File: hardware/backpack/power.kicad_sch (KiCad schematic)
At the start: 13 parts, among them J6 CONN 2x5 P=2.54mm

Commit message: start power
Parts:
- added U5: AP63200WU, Package_TO_SOT_SMD:TSOT-23-6, symbol Regulator_Switching:AP63200WU
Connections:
- net +12V: now also U5.2 (EN), U5.3 (IN)
- net GND: now also U5.4 (GND)

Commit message: start on regs
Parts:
- added C30, C34, C35: 100nF, Capacitor_SMD:C_0603_1608Metric, symbol Device:C_Small
- added C31: 100pF, Capacitor_SMD:C_0603_1608Metric, symbol Device:C_Small
- added C32, C33: 22.0uF, Capacitor_Tantalum_SMD:CP_EIA-3216-10_Kemet-I, symbol Device:C_Polarized_Small
- added F1, F2: 250mA, symbol Device:Polyfuse_Small
- added L3: 6.8uH 2A, symbol Device:L_Ferrite_Small
- added R17: 182K, Resistor_SMD:R_0402_1005Metric, symbol Device:R
- added R18: 62K, Resistor_SMD:R_0402_1005Metric, symbol Device:R
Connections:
- net GND: now also C32.2, C33.2, C34.2, C35.2, R18.1
- net at J6.1 (Pin_1), J6.2 (Pin_2): now also F2.1; no longer D3.1 (K)
- net at J6.10 (Pin_10), J6.9 (Pin_9): now also F1.1; no longer D2.2 (A)
- net at U5.1 (FB): now also C31.1, R17.1, R18.2
- net at U5.5 (SW): now also C30.2, L3.1
- net at U5.6 (BST): now also C30.1
- new net: D3.1 (K), F2.2
- new net: D2.2 (A), F1.2
- new net +3V3: C31.2, C32.1, C33.1, C34.1, C35.1, L3.2, R17.2
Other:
- moved on the sheet: C22, C23, C24, C25, C26, C27, C28, C29, D2, D3, L1, L2

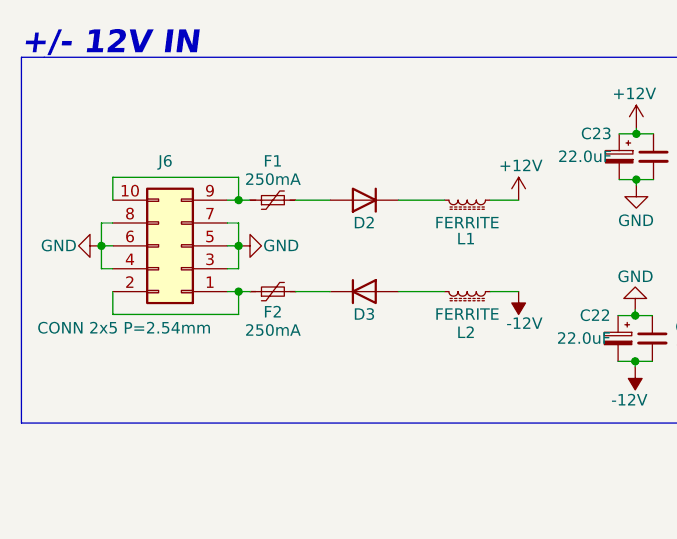
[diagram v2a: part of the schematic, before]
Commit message: parts and capture done sans most needing future pinswaps
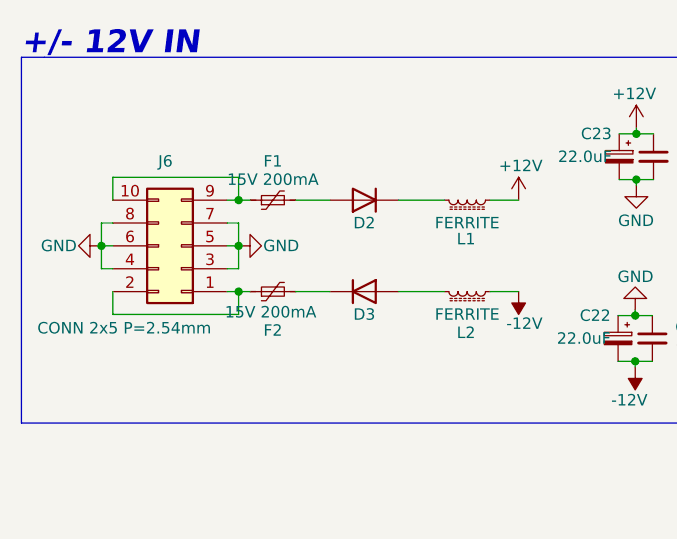
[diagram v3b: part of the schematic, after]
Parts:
- F1, F2: value 250mA -> 15V 200mA; footprint (none) -> Fuse:Fuse_0805_2012Metric; lcsc# (none) -> C883103
- L3: footprint (none) -> Inductor_SMD:L_Vishay_IHLP-2020; lcsc# (none) -> C844992
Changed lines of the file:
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@@
 			)
 		)
-		(property "Footprint" ""
+		(property "Footprint" "Inductor_SMD:L_Vishay_IHLP-2020"
 			(at 86.36 87.63 0)
 			(effects
@@
 			)
 		)
+		(property "lcsc#" " C844992"
+			(at 86.36 87.63 90)
+			(effects
+				(font
+					(size 1.27 1.27)
+				)
+				(hide yes)
+			)
+		)
 		(pin "2"
 		)
@@
 	)
 	(symbol
+		(lib_id "Device:Polyfuse_Small")
+		(at 46.99 46.99 90)
+		(unit 1)
+		(exclude_from_sim no)
+		(in_bom yes)
+		(on_board yes)
+		(dnp no)
+		(property "Reference" "F2"
+			(at 46.99 51.308 90)
+			(effects
+				(font
+					(size 1.27 1.27)
+				)
+			)
+		)
+		(property "Value" "15V 200mA"
+			(at 46.736 49.276 90)
+			(effects
+				(font
+					(size 1.27 1.27)
+				)
+			)
+		)
+		(property "Footprint" "Fuse:Fuse_0805_2012Metric"
+			(at 52.07 45.72 0)
+			(effects
+				(font
+					(size 1.27 1.27)
+				)
+				(justify left)
+				(hide yes)
+			)
+		)
+		(property "Datasheet" "~"
+			(at 46.99 46.99 0)
+			(effects
+				(font
+					(size 1.27 1.27)
+				)
+				(hide yes)
+			)
+		)
+		(property "Description" "Resettable fuse, polymeric positive temperature coefficient, small symbol"
+			(at 46.99 46.99 0)
+			(effects
+				(font
+					(size 1.27 1.27)
+				)
+				(hide yes)
+			)
+		)
+		(property "lcsc#" "C883103"
+			(at 46.99 46.99 90)
+			(effects
+				(font
+					(size 1.27 1.27)
+				)
+				(hide yes)
+			)
+		)
+		(pin "2"
+		)
+		(pin "1"
+		)
+		(instances
+			(project "backpack"
+				(path "/df6062c3-a570-4505-924c-c7fe32df3670/4885642e-e1b2-4a9c-a477-910295b2621e"
+					(reference "F2")
+					(unit 1)
+				)
+			)
+		)
+	)
+	(symbol
 		(lib_id "Device:C_Polarized_Small")
 		(at 85.344 52.197 0)
@@
 	(symbol
 		(lib_id "Device:Polyfuse_Small")
-		(at 46.99 46.99 90)
+		(at 46.99 36.83 90)
 		(unit 1)
 		(exclude_from_sim no)
@@
 		(on_board yes)
 		(dnp no)
-		(property "Reference" "F2"
-			(at 46.99 49.276 90)
+		(property "Reference" "F1"
+			(at 46.99 32.512 90)
 			(effects
 				(font
@@
 			)
 		)
-		(property "Value" "250mA"
-			(at 46.99 51.308 90)
+		(property "Value" "15V 200mA"
+			(at 46.99 34.544 90)
 			(effects
 				(font
@@
 			)
 		)
-		(property "Footprint" ""
-			(at 52.07 45.72 0)
+		(property "Footprint" "Fuse:Fuse_0805_2012Metric"
+			(at 52.07 35.56 0)
 			(effects
 				(font
@@
 		)
 		(property "Datasheet" "~"
-			(at 46.99 46.99 0)
+			(at 46.99 36.83 0)
 			(effects
 				(font
@@
 		)
 		(property "Description" "Resettable fuse, polymeric positive temperature coefficient, small symbol"
-			(at 46.99 46.99 0)
-			(effects
-				(font
-					(size 1.27 1.27)
-				)
-				(hide yes)
-			)
-		)
-		(pin "2"
-		)
-		(pin "1"
-		)
-		(instances
-			(project "backpack"
-				(path "/df6062c3-a570-4505-924c-c7fe32df3670/4885642e-e1b2-4a9c-a477-910295b2621e"
-					(reference "F2")
-					(unit 1)
-				)
-			)
-		)
-	)
-	(symbol
-		(lib_id "Device:Polyfuse_Small")
-		(at 46.99 36.83 90)
-		(unit 1)
-		(exclude_from_sim no)
-		(in_bom yes)
-		(on_board yes)
-		(dnp no)
-		(property "Reference" "F1"
-			(at 46.99 32.512 90)
-			(effects
-				(font
-					(size 1.27 1.27)
-				)
-			)
-		)
-		(property "Value" "250mA"
-			(at 46.99 34.544 90)
-			(effects
-				(font
-					(size 1.27 1.27)
-				)
-			)
-		)
-		(property "Footprint" ""
-			(at 52.07 35.56 0)
-			(effects
-				(font
-					(size 1.27 1.27)
-				)
-				(justify left)
-				(hide yes)
-			)
-		)
-		(property "Datasheet" "~"
 			(at 46.99 36.83 0)
 			(effects
@@
 			)
 		)
-		(property "Description" "Resettable fuse, polymeric positive temperature coefficient, small symbol"
-			(at 46.99 36.83 0)
+		(property "lcsc#" "C883103"
+			(at 46.99 36.83 90)
 			(effects
 				(font

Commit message: aux vin over usb
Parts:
- added C36: 22.0uF, Capacitor_Tantalum_SMD:CP_EIA-3216-10_Kemet-I, symbol Device:C_Polarized_Small
- added D6: 1N4007FL, Diode_SMD:D_SOD-123F, symbol Diode:US1G
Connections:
- net +12V: now also D6.2 (A); no longer U5.2 (EN), U5.3 (IN)
- net GND: now also C36.2
- new net VAUX: C36.1, D6.1 (K), U5.2 (EN), U5.3 (IN)

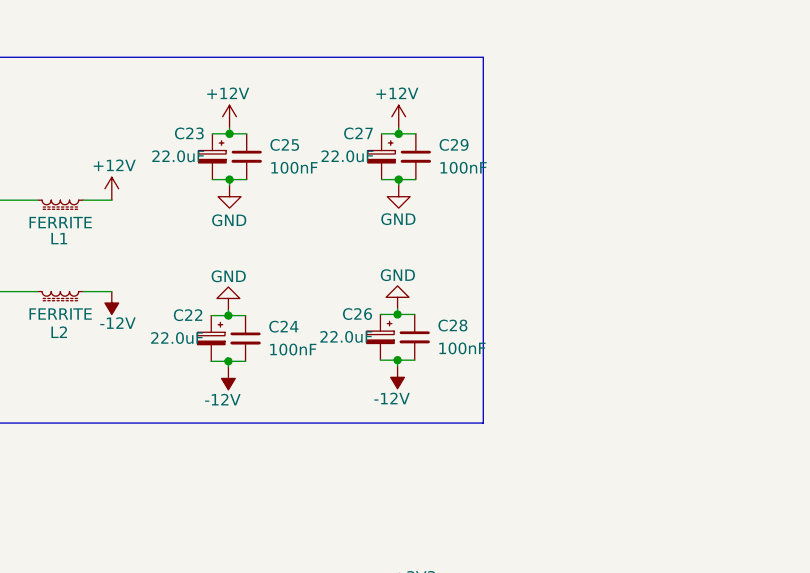
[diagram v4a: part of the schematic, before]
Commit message: connections + placement done
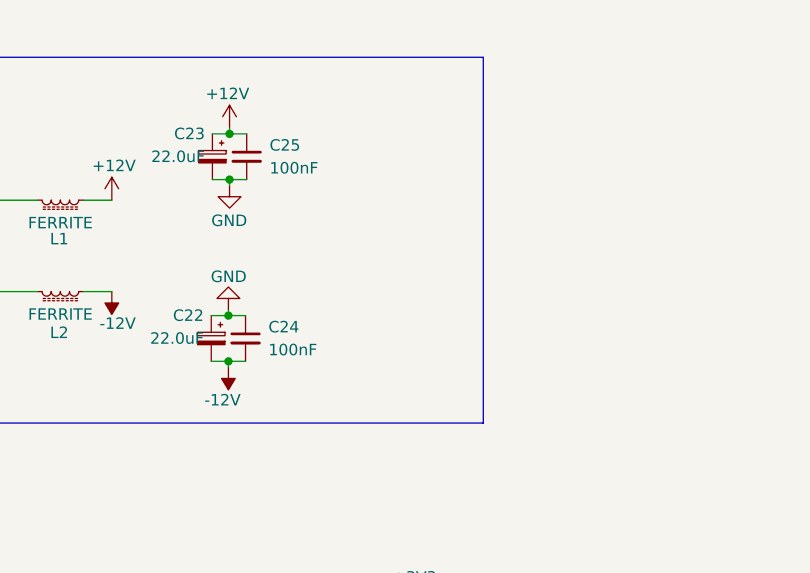
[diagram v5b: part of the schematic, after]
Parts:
- removed C26, C27: 22.0uF, Capacitor_Tantalum_SMD:CP_EIA-3216-10_Kemet-I, symbol Device:C_Polarized_Small
- removed C28, C29: 100nF, Capacitor_SMD:C_0603_1608Metric, symbol Device:C_Small

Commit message: fix footprint errors and pin assignments on ffc
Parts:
- U5: lcsc# (none) -> C2071868
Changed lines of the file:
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@@
+			)
+		)
+		(property "lcsc#" "C2071868"
+			(at 55.88 87.63 0)
+			(effects
+				(font
+					(size 1.27 1.27)
+				)
+				(hide yes)
 			)
 		)

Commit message: updates before fab 04-04-24
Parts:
- C24, C25, C30, C34, C35: lcsc# C338036 -> C14663
- C31: lcsc# C338036 -> C14858
- D2, D3, D6: lcsc# C2840959 -> C493190
- R17: lcsc# C105871 -> C327365
- R18: lcsc# C105871 -> C137950
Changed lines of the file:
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@@
 			)
 		)
-		(property "Datasheet" ""
+		(property "Datasheet" "~"
 			(at 127 90.17 0)
 			(effects
@@
 			)
 		)
-		(property "lcsc#" "C338036"
+		(property "lcsc#" "C14663"
 			(at 89.281 32.004 0)
 			(effects
@@
 			)
 		)
-		(property "lcsc#" "C2840959"
+		(property "lcsc#" "C493190"
 			(at 57.15 46.99 0)
 			(effects
@@
 			)
 		)
-		(property "lcsc#" "C105871"
+		(property "lcsc#" " C137950"
 			(at 101.6 99.06 0)
 			(effects
@@
 			)
 		)
-		(property "lcsc#" "C2840959"
+		(property "lcsc#" "C493190"
 			(at 57.15 36.83 0)
 			(effects
@@
 			)
 		)
-		(property "lcsc#" "C338036"
+		(property "lcsc#" "C14663"
 			(at 135.89 90.17 0)
 			(effects
@@
 			)
 		)
-		(property "lcsc#" "C338036"
+		(property "lcsc#" "C14663"
 			(at 72.39 87.63 0)
 			(effects
@@
 			)
 		)
-		(property "Datasheet" ""
+		(property "Datasheet" "~"
 			(at 85.471 32.004 0)
 			(effects
@@
 			)
 		)
-		(property "lcsc#" "C338036"
+		(property "lcsc#" "C14663"
 			(at 89.154 52.197 0)
 			(effects
@@
 			)
 		)
-		(property "lcsc#" "C2840959"
+		(property "lcsc#" "C493190"
 			(at 26.67 85.09 0)
 			(effects
@@
 			)
 		)
-		(property "lcsc#" "C338036"
+		(property "lcsc#" "C14663"
 			(at 148.59 90.17 0)
 			(effects
@@
 			)
 		)
-		(property "Datasheet" ""
+		(property "Datasheet" "~"
 			(at 41.91 93.98 0)
 			(effects
@@
 			)
 		)
-		(property "Datasheet" ""
+		(property "Datasheet" "~"
 			(at 116.84 90.17 0)
 			(effects
@@
 			)
 		)
-		(property "lcsc#" "C105871"
+		(property "lcsc#" "C327365"
 			(at 101.6 91.44 0)
 			(effects
@@
 			)
 		)
-		(property "Datasheet" ""
+		(property "Datasheet" "~"
 			(at 85.344 52.197 0)
 			(effects
@@
 			)
 		)
-		(property "lcsc#" "C338036"
+		(property "lcsc#" "C14858"
 			(at 92.71 91.44 0)
 			(effects
